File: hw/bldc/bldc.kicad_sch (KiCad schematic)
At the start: 26 parts, among them J1 Conn_01x06, Q1 BSC13DN30NSFD, Q10 BSC13DN30NSFD, Q2 BSC13DN30NSFD, Q7 BSC13DN30NSFD, Q8 BSC13DN30NSFD, Q9 BSC13DN30NSFD, U1 STM32F070F6Px, U2 IR2101, U3 IR2101, U4 IR2101

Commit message: schematic
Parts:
- removed J1: Conn_01x06, symbol Connector_Generic:Conn_01x06
- added C10, C11, C12, C13, C14, C7, C8, C9: 0.1uF, symbol Device:C
- added D4: LED, symbol Device:LED
- added IC1: MP2315SGJ-P, SOT65P280X100-8N, symbol MP2315SGJ-P:MP2315SGJ-P
- added J2: Conn_01x03, symbol Connector_Generic:Conn_01x03
- added L1: 4R7, symbol Device:L
- added R10: 1K, symbol Device:R_US
- added R11, R18, R8: 20R, symbol Device:R_US
- added R12, R13, R7: R_US, symbol Device:R_US
- added R14: 20K, symbol Device:R_US
- added R15: 75K, symbol Device:R_US
- added R16: 200K, symbol Device:R_US
- added R17: 0R, symbol Device:R_US
- added R19, R20, R21, R22, R23, R24, R25, R26, R27: 4K7, symbol Device:R_US
- added R9: 10K, symbol Device:R_US
- added TP1: A, symbol Connector:TestPoint
- added TP2: B, symbol Connector:TestPoint
- added TP3: C, symbol Connector:TestPoint
- added TP4: VIN, symbol Connector:TestPoint
- added TP5: GND, symbol Connector:TestPoint
- added U6: INA138, Package_TO_SOT_SMD:SOT-23-5, symbol Amplifier_Current:INA138
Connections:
- net RSENSE is gone; now on net GND: Q10.1 (S), Q10.2 (S), Q10.3 (S), Q2.1 (S), Q2.2 (S), Q2.3 (S), Q8.1 (S), Q8.2 (S), Q8.3 (S)
- net GND: now also U1.1 (BOOT0), U1.15 (VSS), C10.2, C11.2, C12.2, C14.1, C7.2, C8.2, C9.2, IC1.4 (GND), J2.3 (Pin_3), R13.2, R15.2, R20.2, R23.2, R26.2, R8.1, TP5.1, U6.2 (GND)
- net VDC: now also R17.1, R7.2, U6.4 (-)
- net VDD: now also C9.1, IC1.2 (IN), R16.1, R17.2
- net PHASE_A: now reaches C1.2, C2.2, Q1.1 (S), Q1.2 (S), Q1.3 (S), Q2.5 (D), U2.6 (VS)
- net PHASE_A: now also R19.1, TP1.1
- net PHASE_B: now reaches C3.2, C4.2, Q7.1 (S), Q7.2 (S), Q7.3 (S), Q8.5 (D), U3.6 (VS)
- net PHASE_B: now also R22.1, TP2.1
- net Y_HIN: now reaches U3.2 (HIN)
- net Y_LIN: now reaches U3.3 (LIN)
- net PHASE_C: now reaches C5.2, C6.2, Q10.5 (D), Q9.1 (S), Q9.2 (S), Q9.3 (S), U4.6 (VS)
- net PHASE_C: now also R25.1, TP3.1
- net +3V3: now reaches U1.16 (VDD)
- net +3V3: now also U1.5 (VDDA), C11.1, C14.2, L1.2, R10.1, R12.1, R9.2, U6.5 (V+)
- net at U1.4 (NRST): now also R9.1
- net B_HIN: now reaches U4.2 (HIN)
- net B_LIN: now reaches U4.3 (LIN)
- net R_HIN: now reaches U2.2 (HIN)
- net R_LIN: now reaches U2.3 (LIN)
- new net: R12.2, R13.1, R14.2
- new net: D4.2 (A), R10.2
- new net: C13.2, IC1.3 (SW), L1.1
- new net: IC1.5 (BST), R11.1
- new net: C13.1, R11.2
- new net: IC1.1 (AAM), R15.1
- new net: IC1.6 (EN), R16.2
- new net: C12.1, IC1.7 (VCC)
- new net ADC_A: C7.1, R19.2, R20.1, R21.1
- new net ADC_B: C8.1, R22.2, R23.1, R24.1
- new net ADC_C: C10.1, R25.2, R26.1, R27.1
- new net ADC_CENTER: R21.2, R24.2, R27.2
- new net FB: IC1.8 (FB), R14.1
- new net ISENSE: R8.2, U6.1
- new net LED: D4.1 (K)
- new net VIN: R7.1, TP4.1, U6.3 (+)
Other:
- note removed: "24V to 3.3V / 0.5Amp"
- moved on the sheet: C1, C2, C3, C4, C5, C6, D1, D2, D3, Q1, Q10, Q2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

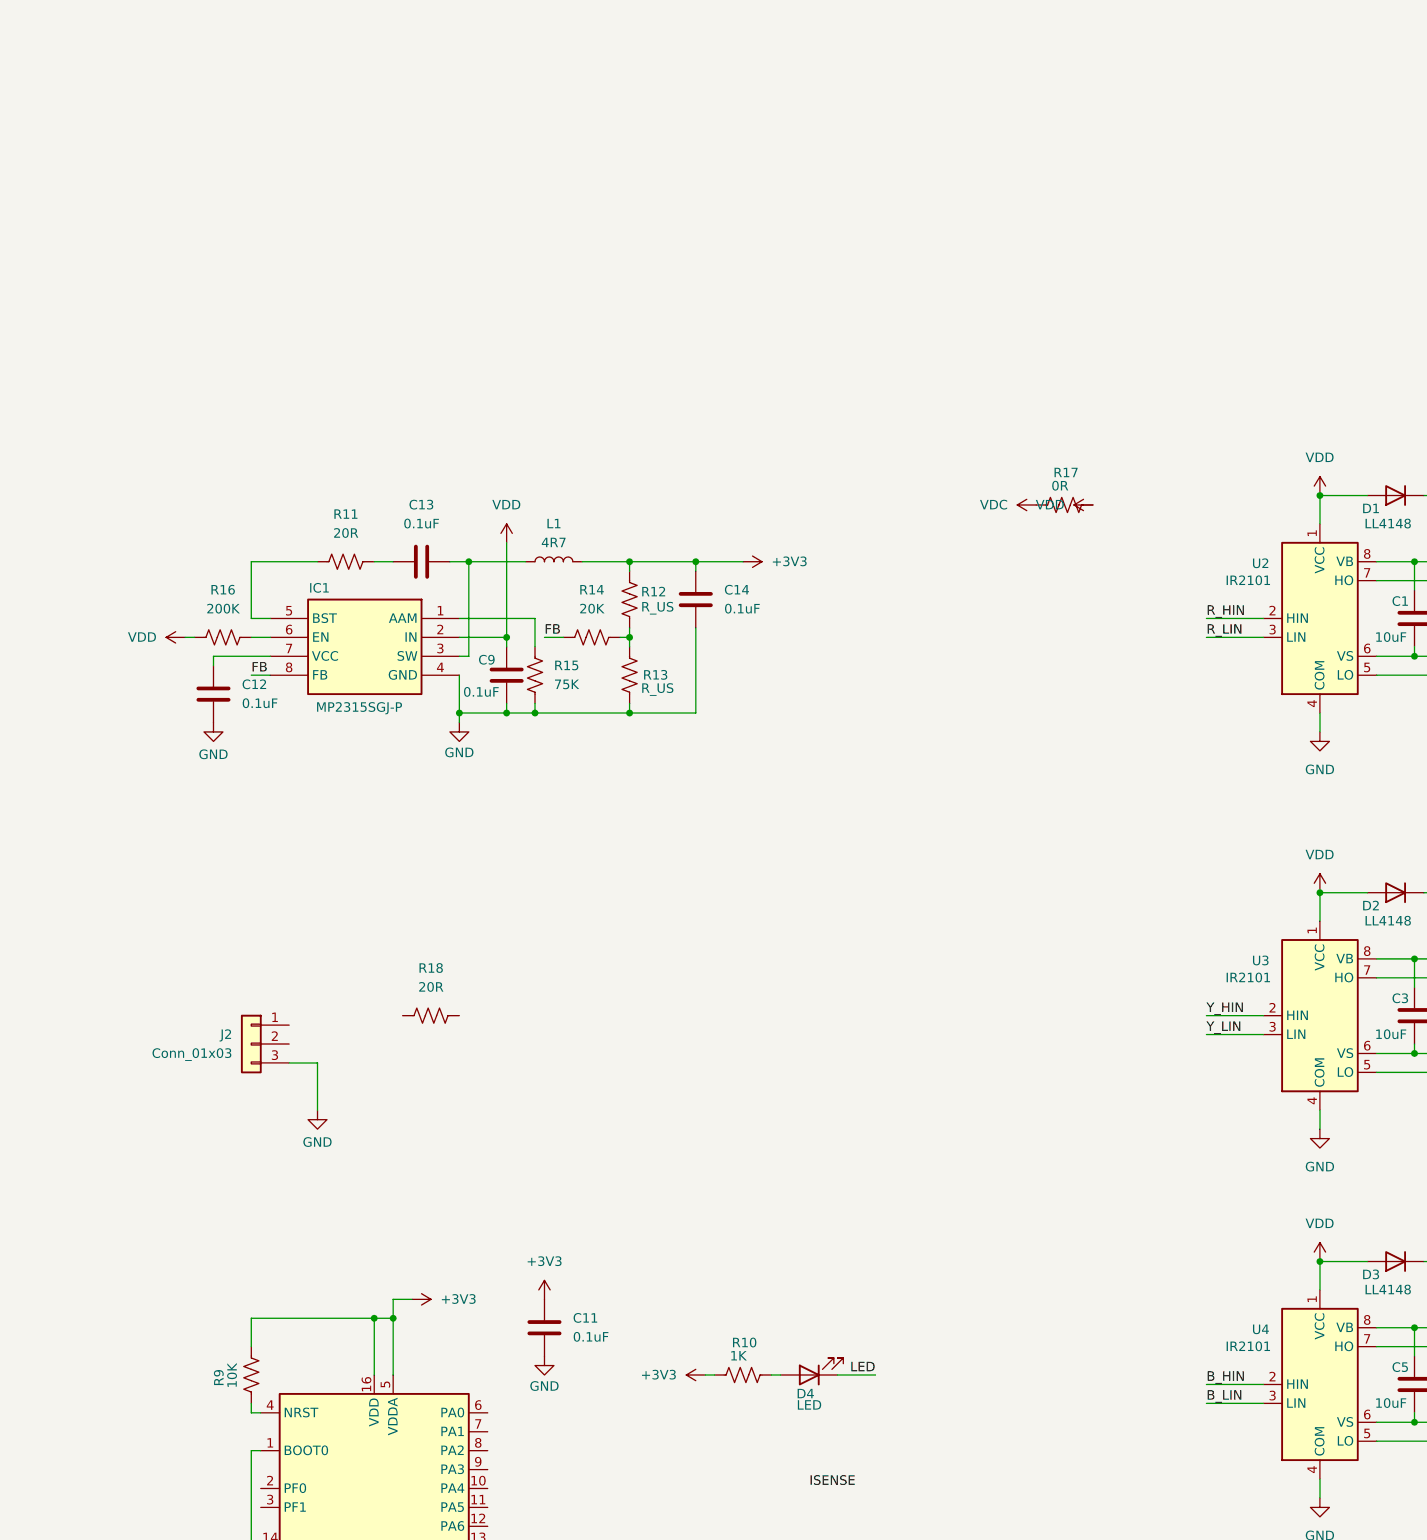
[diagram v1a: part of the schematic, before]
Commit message: schematic update
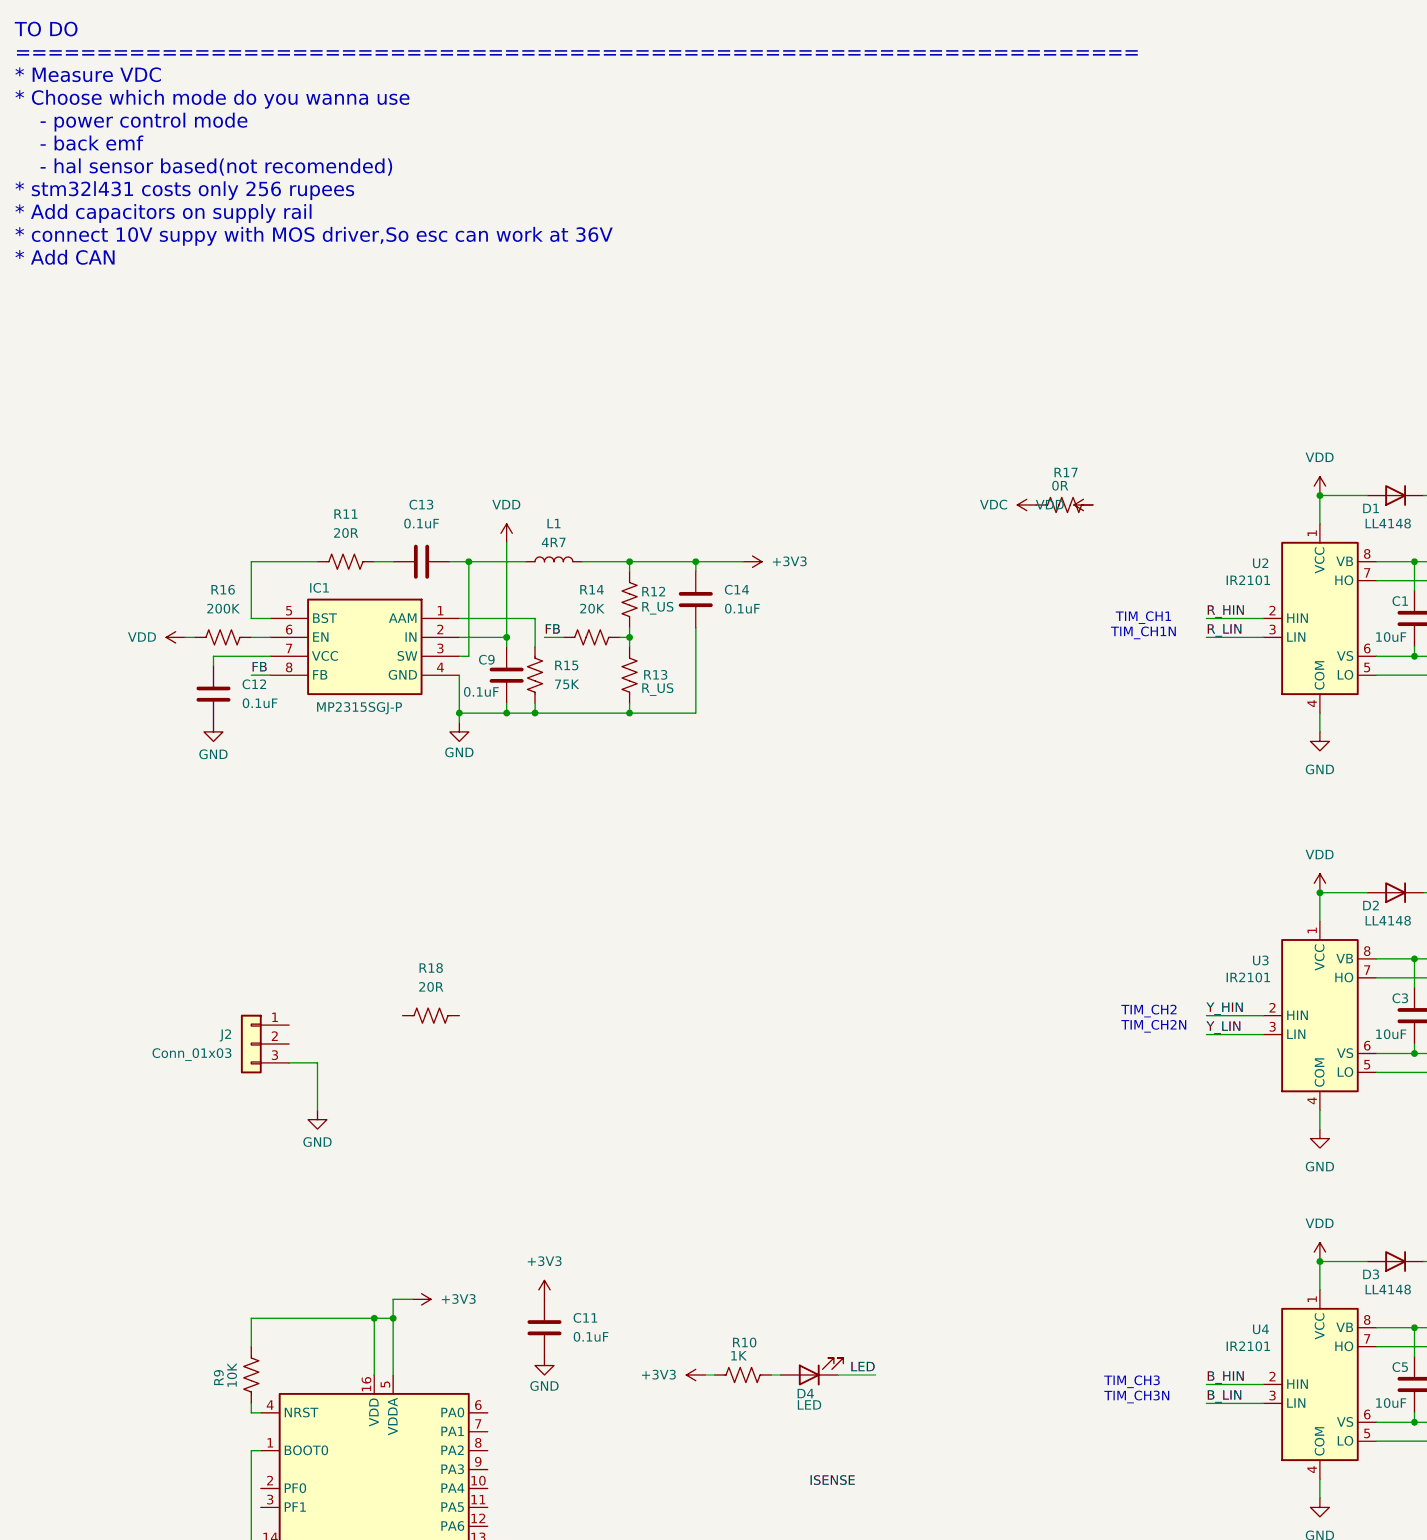
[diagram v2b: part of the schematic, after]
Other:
- note added: "TIM_CH1 TIM_CH1N"
- note added: "TIM_CH2 TIM_CH2N"
- note added: "TIM_CH3 TIM_CH3N"
- note added: "TO DO ===================================================================== * Measure VDC * Choose which mode do you wanna use - power control mode - back emf - hal sensor based(not recomended) * stm32l431 costs only 256 rupees * Add capacitors on supply rail * connect 10V suppy with MOS driver,So esc can work at 36V * Add CAN"
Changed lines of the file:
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@@
+		)
+	)
+	(text "TIM_CH1\nTIM_CH1N\n"
+		(exclude_from_sim no)
+		(at 154.178 36.576 0)
+		(effects
+			(font
+				(size 1.27 1.27)
+			)
+		)
+	)
+	(text "TO DO\n=====================================================================\n* Measure VDC\n* Choose which mode do you wanna use\n	- power control mode\n	- back emf\n	- hal sensor based(not recomended)\n* stm32l431 costs only 256 rupees\n* Add capacitors on supply rail\n* connect 10V suppy with MOS driver,So esc can work at 36V\n* Add CAN"
+		(exclude_from_sim no)
+		(at 2.54 -27.94 0)
+		(effects
+			(font
+				(size 1.905 1.905)
+			)
+			(justify left)
+		)
+	)
+	(text "TIM_CH2\nTIM_CH2N\n"
+		(exclude_from_sim no)
+		(at 151.13 89.408 0)
+		(effects
+			(font
+				(size 1.27 1.27)
+			)
+			(justify left)
+		)
+	)
+	(text "TIM_CH3\nTIM_CH3N\n"
+		(exclude_from_sim no)
+		(at 148.844 139.192 0)
+		(effects
+			(font
+				(size 1.27 1.27)
+			)
+			(justify left)
 		)
 	)

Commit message: sch update using BEMF
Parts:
- added R28: 10K, symbol Device:R_US
- added U5: STM32L431CCTx, Package_QFP:LQFP-48_7x7mm_P0.5mm, symbol MCU_ST_STM32L4:STM32L431CCTx
- R19, R22, R25: value 4K7 -> 100K
- R20, R23, R26: value 4K7 -> 10K
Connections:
- net +3V3: now also R28.2, U5.1 (VBAT), U5.24 (VDD), U5.36 (VDD), U5.48 (VDD), U5.9 (VDDA)
- net GND: now also U5.23 (VSS), U5.35 (VSS), U5.47 (VSS), U5.8 (VSSA)
- new net RESET: R28.1, U5.7 (NRST)
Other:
- note added: "Buck Converter 3.3V"
- note added: "TO DO ===================================================================== * Measure VDC * Choose which mode do you wanna use - power control mode - back emf ( we are using this one) - hal sensor based(not recomended) * stm32l431 costs only 256 rupees * Add capacitors on supply rail * connect 10V suppy with MOS driver,So esc can work at 36V * Add CAN * programming connector * Add a crystal"
- note removed: "TO DO ===================================================================== * Measure VDC * Choose which mode do you wanna use - power control mode - back emf - hal sensor based(not recomended) * stm32l431 costs only 256 rupees * Add capacitors on supply rail * connect 10V suppy with MOS driver,So esc can work at 36V * Add CAN"
- moved on the sheet: C11, C12, C13, C14, C9, D4, IC1, J2, L1, R10, R11, R12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

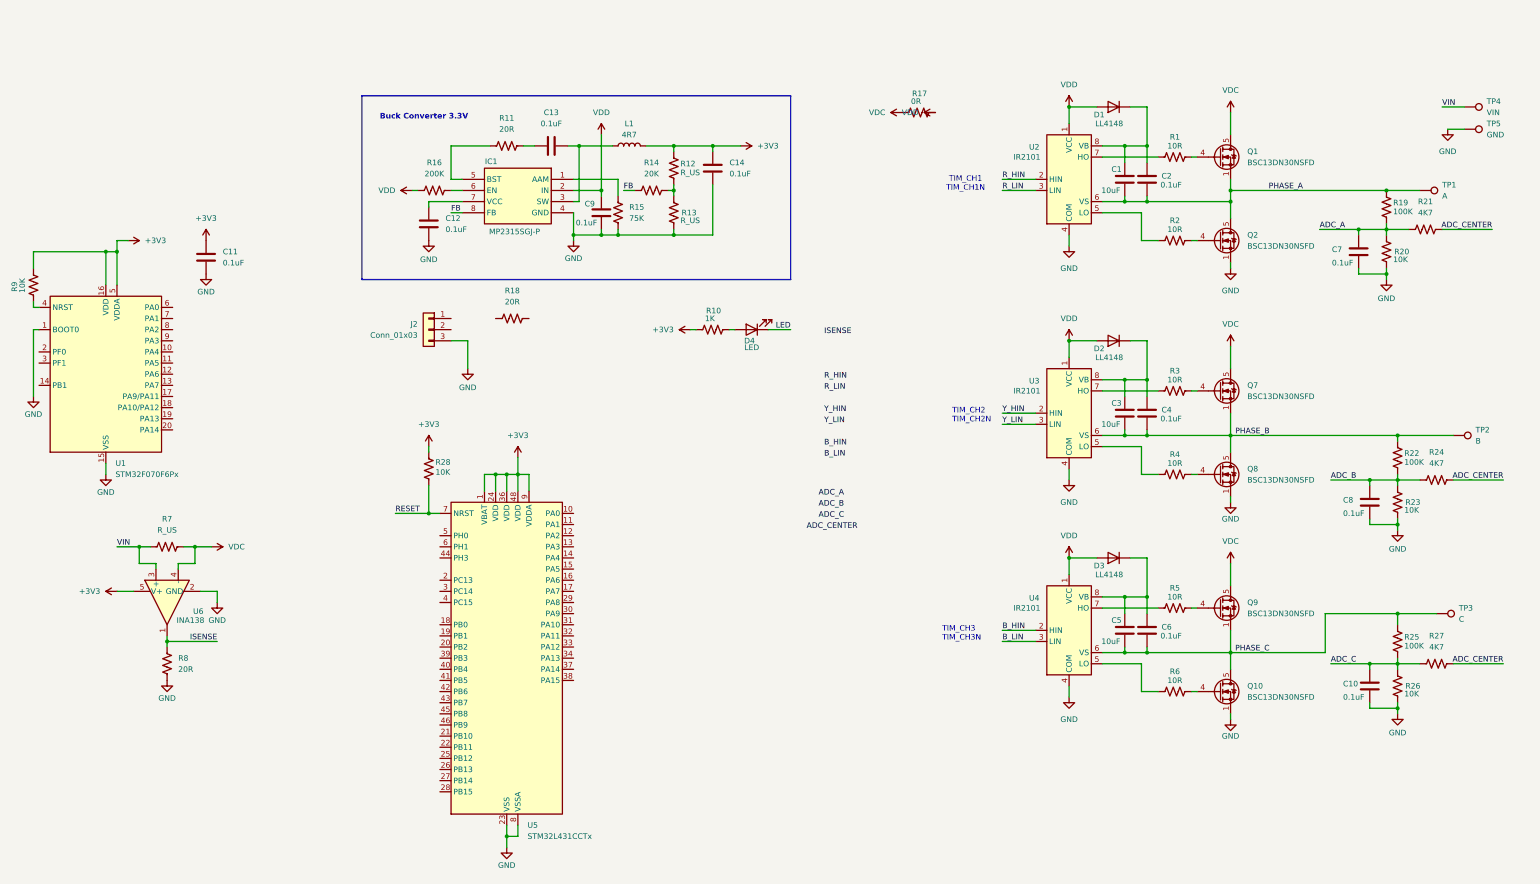
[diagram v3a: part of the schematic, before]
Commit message: schematic update
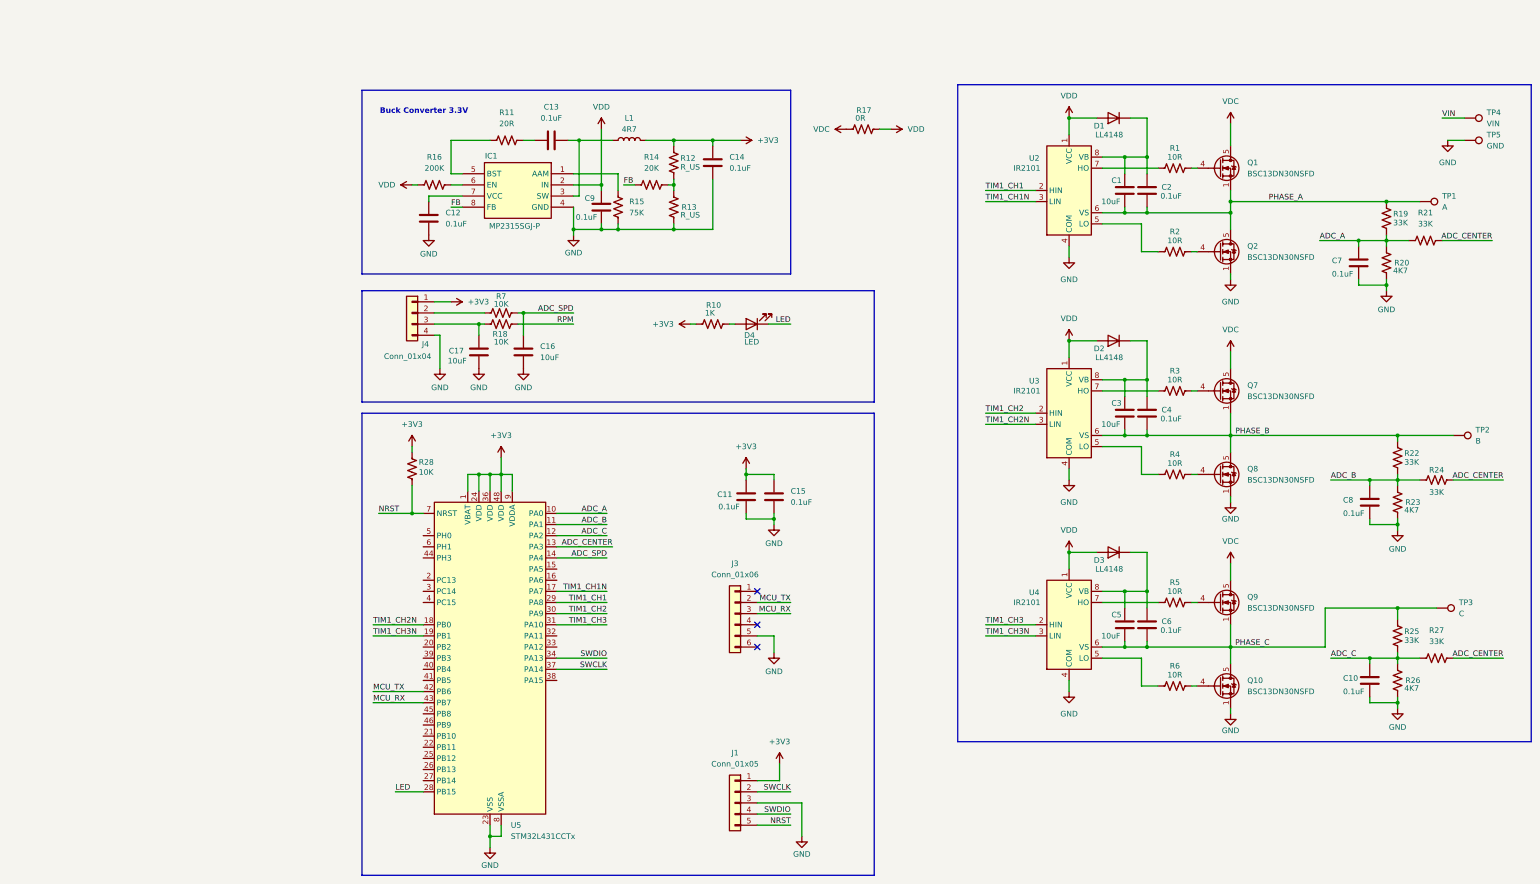
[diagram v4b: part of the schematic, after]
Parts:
- removed J2: Conn_01x03, symbol Connector_Generic:Conn_01x03
- removed R8: 20R, symbol Device:R_US
- removed R9: 10K, symbol Device:R_US
- removed U1: STM32F070F6Px, Package_SO:TSSOP-20_4.4x6.5mm_P0.65mm, symbol MCU_ST_STM32F0:STM32F070F6Px
- removed U6: INA138, Package_TO_SOT_SMD:SOT-23-5, symbol Amplifier_Current:INA138
- added C15: 0.1uF, symbol Device:C
- added C16, C17: 10uF, symbol Device:C
- added J1: Conn_01x05, symbol Connector_Generic:Conn_01x05
- added J3: Conn_01x06, symbol Connector_Generic:Conn_01x06
- added J4: Conn_01x04, symbol Connector_Generic:Conn_01x04
- R18: value 20R -> 10K
- R19, R22, R25: value 100K -> 33K
- R20, R23, R26: value 10K -> 4K7
- R21, R24, R27: value 4K7 -> 33K
- R7: value R_US -> 10K
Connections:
- net B_HIN is gone; now on net TIM1_CH3: U4.2 (HIN)
- net B_LIN is gone; now on net TIM1_CH3N: U4.3 (LIN)
- net R_HIN is gone; now on net TIM1_CH1: U2.2 (HIN)
- net R_LIN is gone; now on net TIM1_CH1N: U2.3 (LIN)
- net Y_HIN is gone; now on net TIM1_CH2: U3.2 (HIN)
- net Y_LIN is gone; now on net TIM1_CH2N: U3.3 (LIN)
- net +3V3: now also C11.2, C15.2, J1.1 (Pin_1), J4.1 (Pin_1); no longer C11.1
- net ADC_A: now also U5.10 (PA0)
- net ADC_B: now also U5.11 (PA1)
- net ADC_C: now also U5.12 (PA2)
- net ADC_CENTER: now also U5.13 (PA3)
- net GND: now also C11.1, C15.1, C16.1, C17.1, J1.3 (Pin_3), J3.5 (Pin_5), J4.4 (Pin_4); no longer C11.2
- net LED: now also U5.28 (PB15)
- net VDC: no longer R7.2
- net VIN: no longer R7.1
- net ADC_SPD: now reaches U5.14 (PA4)
- net ADC_SPD: now also R18.1, C16.2
- net TIM1_CH1N: now reaches U5.17 (PA7)
- net TIM1_CH2N: now reaches U5.18 (PB0)
- net TIM1_CH3N: now reaches U5.19 (PB1)
- net TIM1_CH1: now reaches U5.29 (PA8)
- net TIM1_CH2: now reaches U5.30 (PA9)
- net TIM1_CH3: now reaches U5.31 (PA10)
- net SWDIO: now reaches U5.34 (PA13)
- net SWDIO: now also J1.4 (Pin_4)
- net SWCLK: now reaches U5.37 (PA14)
- net SWCLK: now also J1.2 (Pin_2)
- net MCU_TX: now reaches U5.42 (PB6)
- net MCU_TX: now also J3.2 (Pin_2)
- net MCU_RX: now reaches U5.43 (PB7)
- net MCU_RX: now also J3.3 (Pin_3)
- net at R18.2: now also J4.2 (Pin_2)
- net RESET renamed NRST
- net NRST: now also J1.5 (Pin_5)
- new net: C17.2, J4.3 (Pin_3), R7.2
- new net RPM: R7.1
- no-connect marks 0 -> 3
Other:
- note removed: "TIM_CH1 TIM_CH1N"
- note removed: "TIM_CH2 TIM_CH2N"
- note removed: "TIM_CH3 TIM_CH3N"
- moved on the sheet: C1, C10, C12, C13, C14, C2, C5, C6, C7, C9, D1, D3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
